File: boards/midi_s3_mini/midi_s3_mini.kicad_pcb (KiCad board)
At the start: 2 copper layers, 90 x 70 mm, 102 parts, among them J1 OneButtonA_TX, J10 JOG, J13 PowerIn, J14 TEST_5V, J15 GND_IN, J16 TEST_3V3_S3, J17 TEST_3V3_PERI, J18 GND_PERI, J2 OneButtonA_RX, J3 OneButtonB_RX, J4 OneButtonB_TX, J5 UART_PI, J6 TRACK_ENC, J7 LOOP, J8 PLAY_CUE, J9 TEMPO, Q1 AO3401A, U1 LOLIN_S3_Mini, U2 SPX3819M5-L/TR

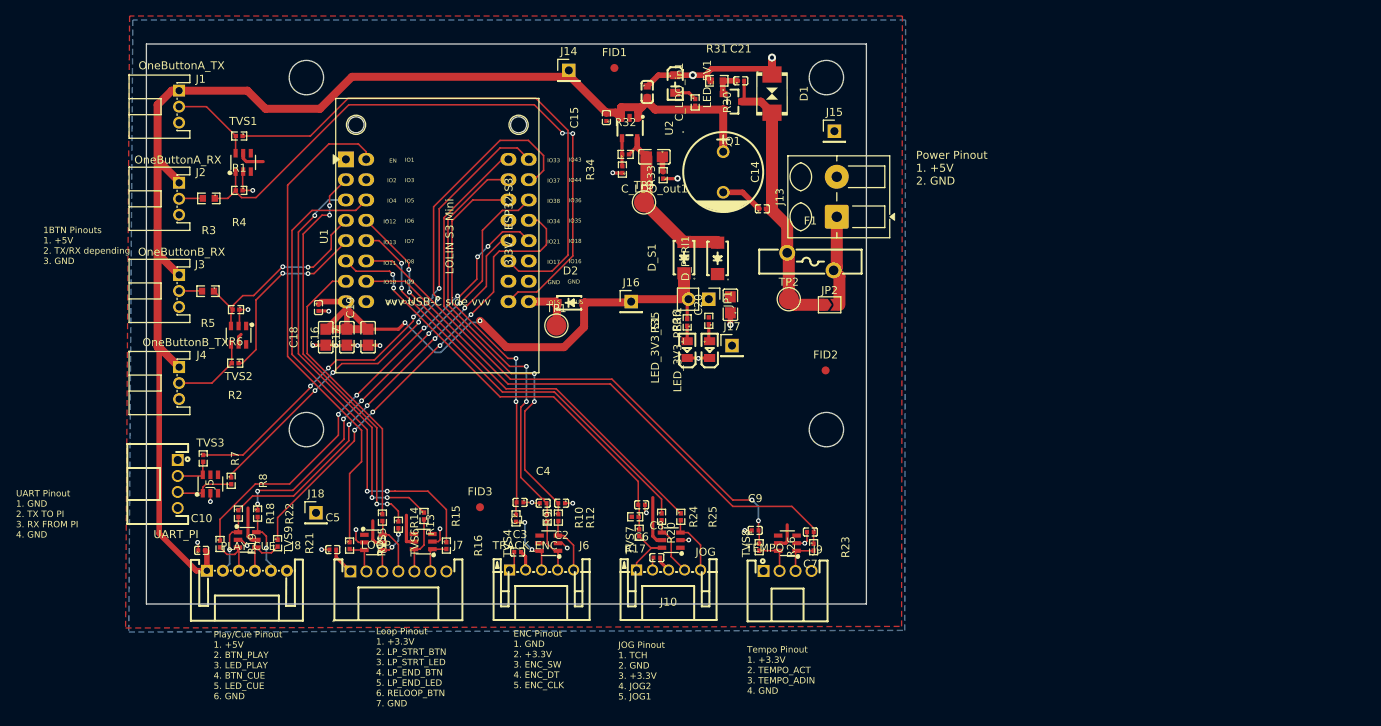
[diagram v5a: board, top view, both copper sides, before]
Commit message: Finish PCB routing, zero DRC errors, silk is left todo
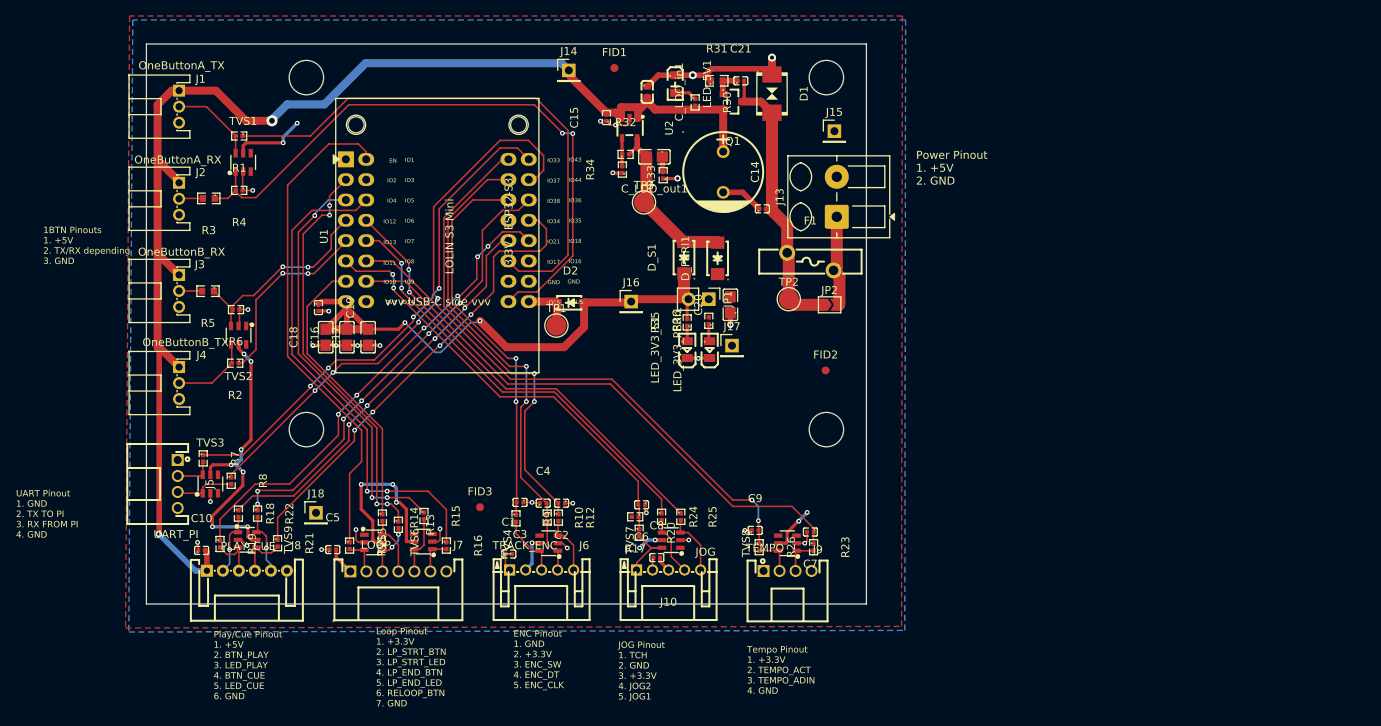
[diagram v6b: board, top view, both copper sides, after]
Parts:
- moved C1 1.13 mm to (65.3, 83.8)
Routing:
- net +3.3V: track 34.9 -> 87.8 mm, vias 0 -> 17
- net GND: track 72.8 -> 78.0 mm, vias 26 -> 28
- net +5V: track 161.2 -> 163.5 mm, vias 0 -> 2
- net /RAW_ENC_SW: track 8.42 -> 7.91 mm, vias 2 -> 0

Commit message: Finish PCB silkscreen and final placement
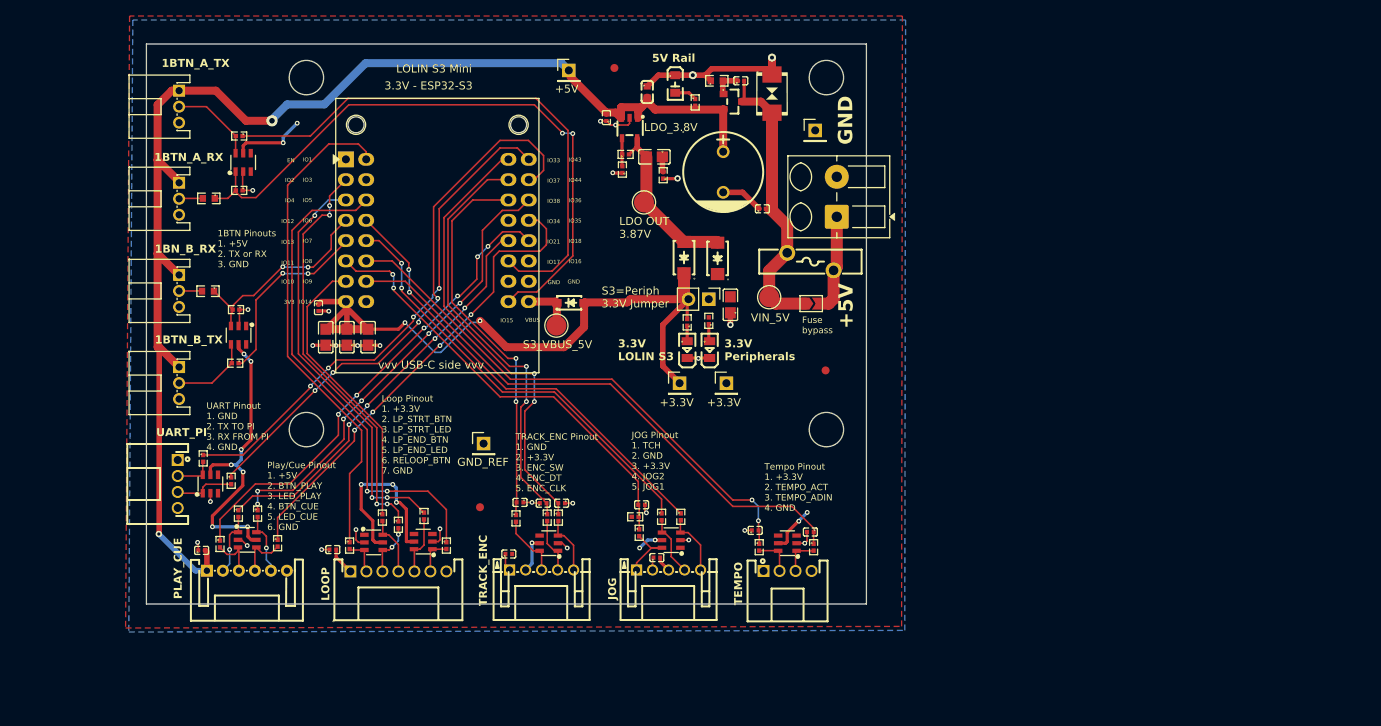
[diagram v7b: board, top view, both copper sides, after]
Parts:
- J1: value OneButtonA_TX -> 1BTN_A_TX
- J2: value OneButtonA_RX -> 1BTN_A_RX
- J3: value OneButtonB_RX -> 1BN_B_RX
- J4: value OneButtonB_TX -> 1BTN_B_TX
- moved J18 22.7 mm to (62.1, 70.0)
- moved J16 11.9 mm to (86.7, 62.4)
- moved J17 4.75 mm to (92.5, 62.4)
- moved TP2 2.46 mm to (97.8, 51.6)
- moved J15 2.40 mm to (103.6, 30.8)
- moved JP2 2.30 mm to (103.1, 52.5)
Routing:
- net S3_3.3V: track 75.7 -> 88.4 mm
- net /Power/VIN_5V: track 36.0 -> 37.0 mm
- net Net-(J13-Pin_1): track 11.5 -> 12.1 mm
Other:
- board text added: "+3.3V"
- board text added: "+5V"
- board text added: "1BTN Pinouts 1. +5V 2. TX or RX 3. GND"
- board text added: "3.3V LOLIN S3"
- board text added: "3.3V Peripherals"
- board text added: "5V Rail"
- board text added: "Fuse bypass"
- board text added: "GND"
- board text added: "GND_REF"
- board text added: "LDO OUT 3.87V"
- board text added: "LDO_3.8V"
- board text added: "S3=Periph 3.3V Jumper"
- board text added: "S3_VBUS_5V"
- board text added: "TRACK_ENC Pinout 1. GND 2. +3.3V 3. ENC_SW 4. ENC_DT 5. ENC_CLK"
- board text added: "VIN_5V"
- board text removed: "1BTN Pinouts 1. +5V 2. TX/RX depending 3. GND"
- board text removed: "ENC Pinout 1. GND 2. +3.3V 3. ENC_SW 4. ENC_DT 5. ENC_CLK"
- board text removed: "Power Pinout 1. +5V 2. GND"
